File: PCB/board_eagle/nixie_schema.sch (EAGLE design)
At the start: 93 parts, among them Q1 BC856B, Q2 IRF740S, U2 MC7940N

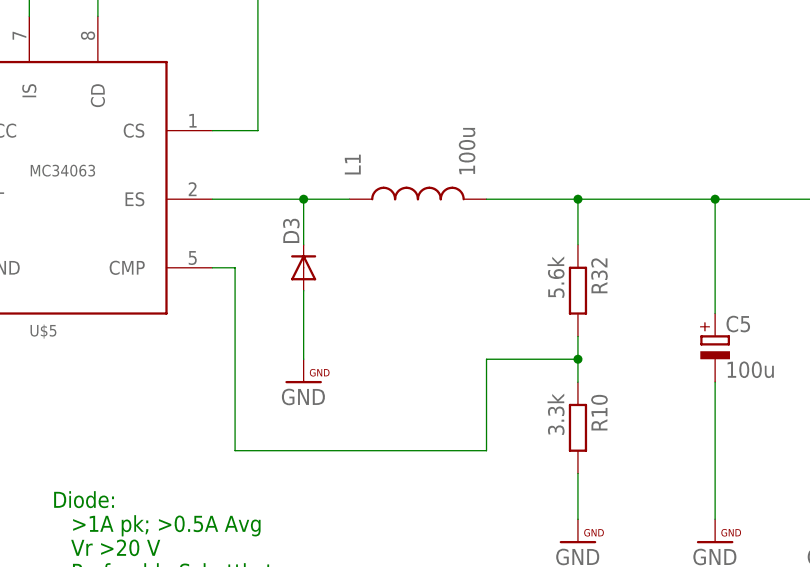
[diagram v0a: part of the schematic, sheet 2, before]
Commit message: Added some footprints
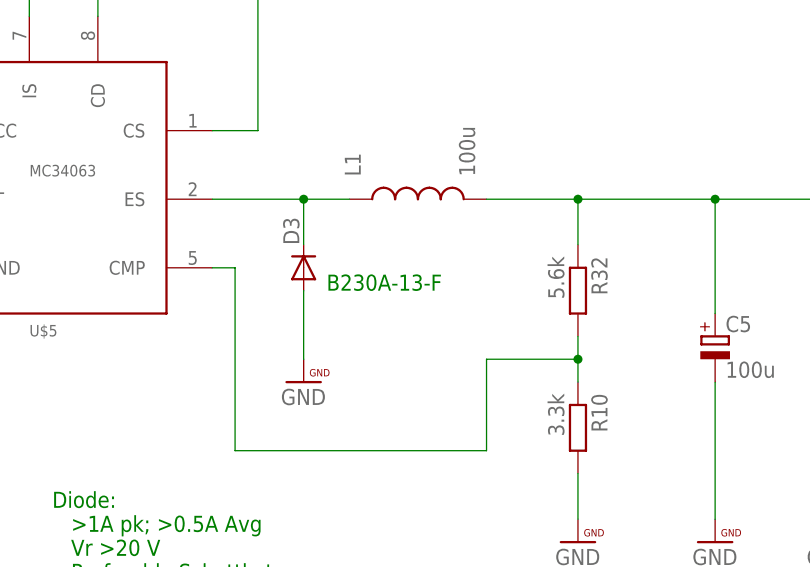
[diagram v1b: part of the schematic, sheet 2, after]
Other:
- note added: "B230A-13-F"
- note added: "ECS-.327-7-34B"
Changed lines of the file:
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@@
    &gt;0.5A cont, &gt;1A peak
    &gt;=100 uH</text>
+<text x="83.82" y="58.42" size="1.778" layer="91">
+B230A-13-F
+</text>
 </plain>
 <instances>
@@
 Note:
    Populate either R8 or R28, not both</text>
+<text x="266.7" y="0" size="1.778" layer="91">
+ECS-.327-7-34B
+</text>
 </plain>
 <instances>

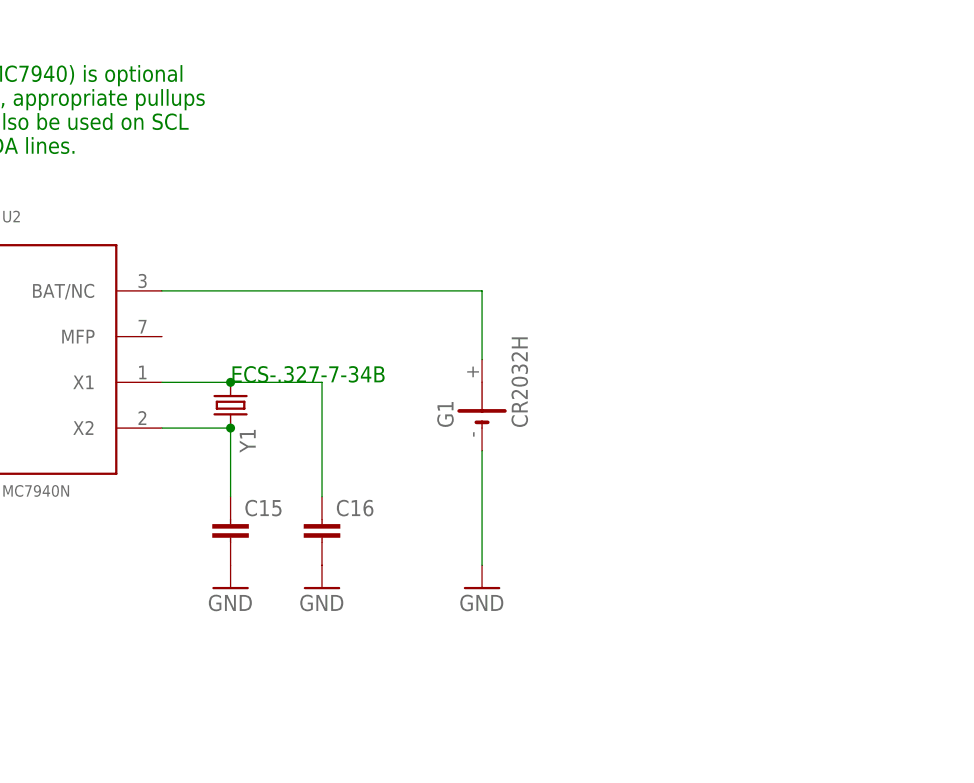
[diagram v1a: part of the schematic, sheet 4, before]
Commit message: Added some more component footprints
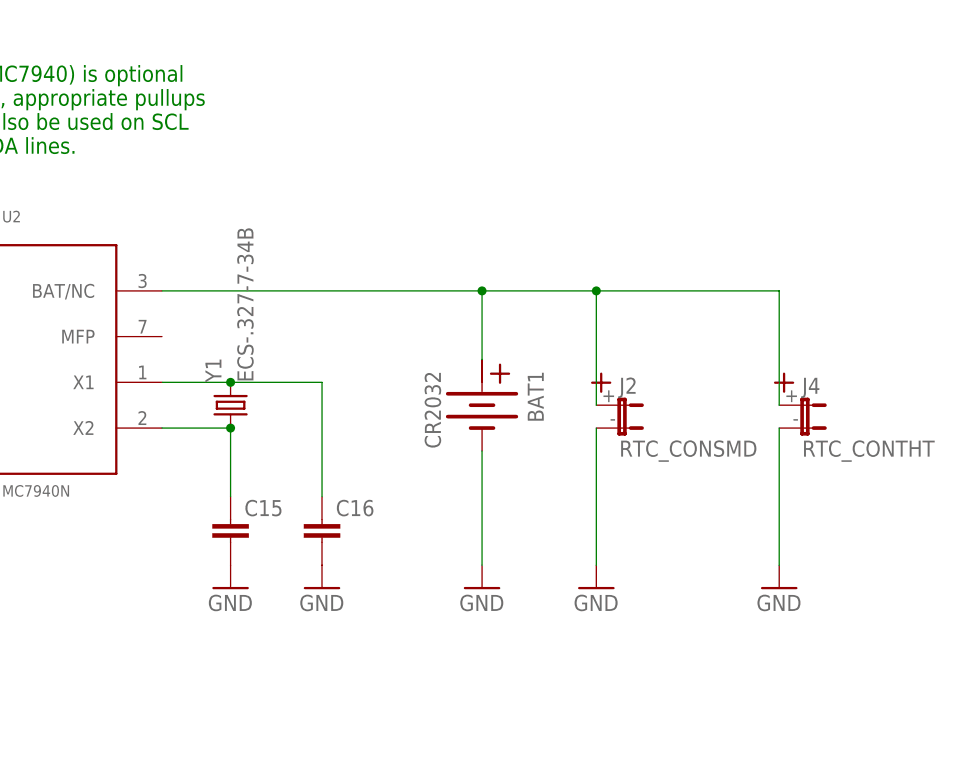
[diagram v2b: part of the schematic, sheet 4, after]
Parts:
- removed G1: CR2032H, battery:CR2032H
- added BAT1: CR2032, nixe_cmp:CR2032
- added D4: B230A-13-F, nixe_cmp:B230A-13-F
- added J2: RTC_CONSMD, nixe_cmp:RTC_CONSMD
- added J4: RTC_CONTHT, nixe_cmp:RTC_CONTHT
- added J5: (no value), con-jack:JACK-PLUG0
- D3: value (none) -> B230A-13-F; device diode:DIODE-SOD123 -> nixe_cmp:B230A-13-F
- Y1: value (none) -> ECS-.327-7-34B; device crystal:CRYSTALSM49 -> nixe_cmp:ECS-.327-7-34B
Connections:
- new net N$93: D4.A, J5.3
- net GND: now also BAT1.-, J2.-, J4.-, J5.1, J5.2; no longer G1.-
- net N$100: now also Y1.1; no longer Y1.2
- net N$22: now also BAT1.+, J2.+, J4.+; no longer G1.+
- net N$99: now also Y1.2; no longer Y1.1
- net VCC: now also D4.C
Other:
- note removed: "B230A-13-F"
- note removed: "ECS-.327-7-34B"
- moved on the sheet: Y1
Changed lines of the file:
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@@
 <part name="U$8" library="PatternAgents-Beautify" deviceset="GND" device=""/>
 <part name="U$9" library="PatternAgents-Beautify" deviceset="GND" device=""/>
-<part name="D3" library="diode" deviceset="DIODE-" device="SOD123"/>
 <part name="C6" library="rcl" deviceset="CPOL-EU" device="153CLV-1014" value="100u"/>
 <part name="U$10" library="PatternAgents-Beautify" deviceset="GND" device=""/>
@@
 <part name="U2" library="nixe_cmp" deviceset="MC7940" device="" technology="N"/>
 <part name="GND11" library="supply1" deviceset="GND" device=""/>
-<part name="G1" library="battery" deviceset="CR2032H" device=""/>
 <part name="GND12" library="supply1" deviceset="GND" device=""/>
 <part name="GND13" library="supply1" deviceset="GND" device=""/>
 <part name="U$11" library="PatternAgents-Beautify" deviceset="GND" device=""/>
 <part name="U$12" library="PatternAgents-Beautify" deviceset="GND" device=""/>
-<part name="Y1" library="crystal" deviceset="CRYSTAL" device="SM49"/>
 <part name="C15" library="rcl" deviceset="C-EU" device="C0805"/>
 <part name="C16" library="rcl" deviceset="C-EU" device="C0805"/>
@@
 <part name="U$31" library="PatternAgents-Beautify" deviceset="GND" device=""/>
 <part name="R8" library="resistor" deviceset="R-EU_" device="R0603"/>
+<part name="Y1" library="nixe_cmp" deviceset="ECS-.327-7-34B" device=""/>
+<part name="BAT1" library="nixe_cmp" deviceset="CR2032" device=""/>
+<part name="J2" library="nixe_cmp" deviceset="RTC_CON" device="SMD"/>
+<part name="J4" library="nixe_cmp" deviceset="RTC_CON" device="THT"/>
+<part name="GND16" library="supply1" deviceset="GND" device=""/>
+<part name="GND17" library="supply1" deviceset="GND" device=""/>
+<part name="SUPPLY6" library="SparkFun-PowerSymbols" deviceset="VCC" device=""/>
+<part name="D3" library="nixe_cmp" deviceset="B230A-13-F" device=""/>
+<part name="D4" library="nixe_cmp" deviceset="B230A-13-F" device=""/>
+<part name="J5" library="con-jack" deviceset="JACK-PLUG" device="0"/>
+<part name="U$32" library="PatternAgents-Beautify" deviceset="GND" device=""/>
 </parts>
 <sheets>
@@
    &gt;0.5A cont, &gt;1A peak
    &gt;=100 uH</text>
-<text x="83.82" y="58.42" size="1.778" layer="91">
-B230A-13-F
-</text>
 </plain>
 <instances>
@@
 <instance part="U$8" gate="G$1" x="111.76" y="33.02"/>
 <instance part="U$9" gate="G$1" x="81.28" y="50.8"/>
-<instance part="D3" gate="G$1" x="81.28" y="60.96" rot="R90"/>
 <instance part="C6" gate="G$1" x="139.7" y="53.34"/>
 <instance part="U$10" gate="G$1" x="139.7" y="33.02"/>
@@
 <instance part="C8" gate="G$1" x="0" y="53.34"/>
 <instance part="C4" gate="G$1" x="12.7" y="53.34"/>
+<instance part="SUPPLY6" gate="G$1" x="-10.16" y="111.76"/>
+<instance part="D3" gate="G$1" x="81.28" y="60.96" rot="R90"/>
+<instance part="D4" gate="G$1" x="-25.4" y="83.82"/>
+<instance part="J5" gate="G$1" x="-45.72" y="81.28"/>
+<instance part="U$32" gate="G$1" x="-35.56" y="33.02"/>
 </instances>
 <busses>
@@
 <segment>
 <pinref part="U$9" gate="G$1" pin="GND"/>
+<wire x1="81.28" y1="50.8" x2="81.28" y2="58.42" width="0.1524" layer="91"/>
 <pinref part="D3" gate="G$1" pin="A"/>
-<wire x1="81.28" y1="50.8" x2="81.28" y2="58.42" width="0.1524" layer="91"/>
 </segment>
 <segment>
@@
 <wire x1="0" y1="33.02" x2="0" y2="48.26" width="0.1524" layer="91"/>
 </segment>
+<segment>
+<pinref part="U$32" gate="G$1" pin="GND"/>
+<wire x1="-35.56" y1="33.02" x2="-35.56" y2="78.74" width="0.1524" layer="91"/>
+<pinref part="J5" gate="G$1" pin="2"/>
+<wire x1="-35.56" y1="78.74" x2="-35.56" y2="81.28" width="0.1524" layer="91"/>
+<wire x1="-35.56" y1="81.28" x2="-40.64" y2="81.28" width="0.1524" layer="91"/>
+<pinref part="J5" gate="G$1" pin="1"/>
+<wire x1="-40.64" y1="78.74" x2="-35.56" y2="78.74" width="0.1524" layer="91"/>
+<junction x="-35.56" y="78.74"/>
+</segment>
 </net>
 <net name="N$12" class="0">
@@
 <pinref part="L1" gate="G$1" pin="1"/>
 <wire x1="71.12" y1="68.58" x2="81.28" y2="68.58" width="0.1524" layer="91"/>
-<pinref part="D3" gate="G$1" pin="C"/>
 <wire x1="81.28" y1="68.58" x2="86.36" y2="68.58" width="0.1524" layer="91"/>
 <wire x1="81.28" y1="63.5" x2="81.28" y2="68.58" width="0.1524" layer="91"/>
 <junction x="81.28" y="68.58"/>
+<pinref part="D3" gate="G$1" pin="C"/>
 </segment>
 </net>
@@
 <wire x1="0" y1="76.2" x2="12.7" y2="76.2" width="0.1524" layer="91"/>
 <junction x="12.7" y="76.2"/>
+</segment>
+<segment>
+<pinref part="SUPPLY6" gate="G$1" pin="VCC"/>
+<wire x1="-22.86" y1="83.82" x2="-10.16" y2="83.82" width="0.1524" layer="91"/>
+<wire x1="-10.16" y1="83.82" x2="-10.16" y2="111.76" width="0.1524" layer="91"/>
+<pinref part="D4" gate="G$1" pin="C"/>
+</segment>
+</net>
+<net name="N$93" class="0">
+<segment>
+<pinref part="J5" gate="G$1" pin="3"/>
+<pinref part="D4" gate="G$1" pin="A"/>
+<wire x1="-40.64" y1="83.82" x2="-27.94" y2="83.82" width="0.1524" layer="91"/>
 </segment>
 </net>
@@
 Note:
    Populate either R8 or R28, not both</text>
-<text x="266.7" y="0" size="1.778" layer="91">
-ECS-.327-7-34B
-</text>
 </plain>
 <instances>
@@
 <instance part="U2" gate="G$1" x="243.84" y="2.54"/>
 <instance part="GND11" gate="1" x="226.06" y="-22.86"/>
-<instance part="G1" gate="1" x="294.64" y="-2.54" rot="R90"/>
 <instance part="GND12" gate="1" x="294.64" y="-22.86"/>
 <instance part="GND13" gate="1" x="215.9" y="7.62"/>
-<instance part="Y1" gate="G$1" x="266.7" y="-2.54" rot="R270"/>
 <instance part="C15" gate="G$1" x="266.7" y="-15.24"/>
 <instance part="C16" gate="G$1" x="276.86" y="-15.24"/>
@@
 <instance part="U$31" gate="G$1" x="-15.24" y="35.56"/>
 <instance part="R8" gate="G$1" x="73.66" y="76.2" rot="R270"/>
+<instance part="Y1" gate="G$1" x="266.7" y="-2.54" rot="R90"/>
+<instance part="BAT1" gate="G$1" x="294.64" y="-2.54" rot="R270"/>
+<instance part="J2" gate="G$1" x="309.88" y="-2.54" rot="R270"/>
+<instance part="J4" gate="G$1" x="330.2" y="-2.54" rot="R270"/>
+<instance part="GND16" gate="1" x="307.34" y="-22.86"/>
+<instance part="GND17" gate="1" x="327.66" y="-22.86"/>
 </instances>
 <busses>
@@
 <segment>
 <pinref part="GND12" gate="1" pin="GND"/>
-<pinref part="G1" gate="1" pin="-"/>
 <wire x1="294.64" y1="-20.32" x2="294.64" y2="-7.62" width="0.1524" layer="91"/>
+<pinref part="BAT1" gate="G$1" pin="-"/>
 </segment>
 <segment>
@@
 <pinref part="C18" gate="G$1" pin="2"/>
 <wire x1="-15.24" y1="35.56" x2="-15.24" y2="40.64" width="0.1524" layer="91"/>
+</segment>
+<segment>
+<pinref part="GND16" gate="1" pin="GND"/>
+<pinref part="J2" gate="G$1" pin="-"/>
+<wire x1="307.34" y1="-20.32" x2="307.34" y2="-5.08" width="0.1524" layer="91"/>
+</segment>
+<segment>
+<pinref part="J4" gate="G$1" pin="-"/>
+<pinref part="GND17" gate="1" pin="GND"/>
+<wire x1="327.66" y1="-5.08" x2="327.66" y2="-20.32" width="0.1524" layer="91"/>
 </segment>
 </net>
@@
 <net name="N$22" class="0">
 <segment>
-<pinref part="G1" gate="1" pin="+"/>
 <wire x1="294.64" y1="2.54" x2="294.64" y2="10.16" width="0.1524" layer="91"/>
 <pinref part="U2" gate="G$1" pin="BAT/NC"/>
 <wire x1="294.64" y1="10.16" x2="259.08" y2="10.16" width="0.1524" layer="91"/>
+<pinref part="BAT1" gate="G$1" pin="+"/>
+<pinref part="J2" gate="G$1" pin="+"/>
+<wire x1="307.34" y1="-2.54" x2="307.34" y2="10.16" width="0.1524" layer="91"/>
+<wire x1="307.34" y1="10.16" x2="294.64" y2="10.16" width="0.1524" layer="91"/>
+<junction x="294.64" y="10.16"/>
+<pinref part="J4" gate="G$1" pin="+"/>
+<wire x1="307.34" y1="10.16" x2="327.66" y2="10.16" width="0.1524" layer="91"/>
+<wire x1="327.66" y1="10.16" x2="327.66" y2="-2.54" width="0.1524" layer="91"/>
+<junction x="307.34" y="10.16"/>
 </segment>
 </net>
@@
 <segment>
 <pinref part="U2" gate="G$1" pin="X1"/>
-<pinref part="Y1" gate="G$1" pin="1"/>
-<wire x1="259.08" y1="0" x2="266.7" y2="0" width="0.1524" layer="91"/>
 <pinref part="C16" gate="G$1" pin="1"/>
 <wire x1="276.86" y1="-12.7" x2="276.86" y2="0" width="0.1524" layer="91"/>
 <wire x1="276.86" y1="0" x2="266.7" y2="0" width="0.1524" layer="91"/>
+<pinref part="Y1" gate="G$1" pin="2"/>
+<wire x1="266.7" y1="0" x2="259.08" y2="0" width="0.1524" layer="91"/>
 <junction x="266.7" y="0"/>
 </segment>
@@
 <segment>
 <pinref part="U2" gate="G$1" pin="X2"/>
-<pinref part="Y1" gate="G$1" pin="2"/>
 <wire x1="259.08" y1="-5.08" x2="266.7" y2="-5.08" width="0.1524" layer="91"/>
 <pinref part="C15" gate="G$1" pin="1"/>
 <wire x1="266.7" y1="-12.7" x2="266.7" y2="-5.08" width="0.1524" layer="91"/>
+<pinref part="Y1" gate="G$1" pin="1"/>
 <junction x="266.7" y="-5.08"/>
 </segment>

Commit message: Starting to do layout
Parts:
- C2: device rcl:CPOL-EU140CLH-0810 -> rcl:C-EUC0805
- S1, S2, S3, S4, S5, S6: value TAC_SWITCHSMD -> (none); device SparkFun-Retired:TAC_SWITCHSMD -> switch-omron:31-XX
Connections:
- net N$86 renamed V_PULSE
- new net N$94: SV7.11
- net +3V3: now also C7.1
- net BUTTON1: now also S3.S; no longer S2.3, S2.4
- net BUTTON2: now also S4.S; no longer S3.3, S3.4
- net BUTTON3: now also S5.S; no longer S4.3, S4.4
- net BUTTON4: now also S6.S; no longer S5.3, S5.4
- net GND: now also C1.2, C10.2, C11.2, C14.2, C2.2, C3.2, C4.2, C8.2, S1.P, S2.P, S3.P, S4.P, S5.P, S6.P; no longer C2.-, S1.1, S1.2, S2.1, S2.2, S3.1, S3.2, S4.1, S4.2, S5.1, S5.2, S6.3, S6.4
- net N$10: no longer SV7.11
- net N$12: now also C4.1
- net N$14: now also S1.S; no longer S1.3, S1.4
- net N$15: now also S2.S; no longer S6.1, S6.2
- net N$74: now also C10.1
- net N$96: now also C11.1
- net VCC: now also C1.1, C14.1, C2.1, C3.1, C8.1; no longer C2.+

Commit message: Some more routing
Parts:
- C12: device rcl:CPOL-EU153CLV-0810 -> rcl:CPOL-EU153CLV-1014
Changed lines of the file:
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@@
 </variantdefs>
 <classes>
-<class number="0" name="default" width="0.1524" drill="0.4064">
-<clearance class="0" value="0.1524"/>
+<class number="0" name="default" width="0.254" drill="0.4">
+<clearance class="0" value="0.2032"/>
 </class>
-<class number="1" name="Power" width="1.016" drill="0.4064">
+<class number="1" name="Power" width="1.016" drill="0.5">
 </class>
-<class number="2" name="HV" width="0.1524" drill="0.4064">
-<clearance class="2" value="0.508"/>
+<class number="2" name="HV" width="0.254" drill="0.5">
+<clearance class="2" value="1"/>
 </class>
 </classes>
@@
 <part name="Q1" library="nixe_cmp" deviceset="BC856B" device=""/>
 <part name="L3" library="nixe_cmp" deviceset="HM78D-128151KLFTR" device="" value="150u"/>
-<part name="C12" library="rcl" deviceset="CPOL-EU" device="153CLV-0810" value="220u"/>
 <part name="C13" library="rcl" deviceset="CPOL-EU" device="153CLV-1014" value="2.2u"/>
 <part name="R27" library="pot" deviceset="TRIM_EU-" device="SM-42/43X" value="100k"/>
@@
 <part name="S1" library="switch-omron" deviceset="31-XX" device=""/>
 <part name="C2" library="rcl" deviceset="C-EU" device="C0805" value="100n"/>
+<part name="C12" library="rcl" deviceset="CPOL-EU" device="153CLV-1014" value="220u"/>
 </parts>
 <sheets>
@@
 <instance part="Q1" gate="Q$1" x="96.52" y="25.4"/>
 <instance part="L3" gate="G$1" x="119.38" y="66.04"/>
-<instance part="C12" gate="G$1" x="88.9" y="66.04"/>
 <instance part="C13" gate="G$1" x="218.44" y="17.78"/>
 <instance part="R27" gate="1" x="200.66" y="17.78"/>
@@
 <instance part="C10" gate="G$1" x="10.16" y="22.86"/>
 <instance part="C11" gate="G$1" x="160.02" y="20.32"/>
+<instance part="C12" gate="G$1" x="88.9" y="66.04"/>
 </instances>
 <busses>

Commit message: Routing the PCB
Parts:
- removed C2: 100n, rcl:C-EUC0805
- removed C9: 10u, rcl:CPOL-EU140CLH-0810
- added P1: 100k, nixe_cmp:UNIVERSAL-POTENTIOMETER_SMD
- added R31, R33, R34, R35: 68k, rcl:R-EU_R0603
- added R36: (no value), resistor:R-EU_R0603
- added T1: PHOTO_TRANS, nixe_cmp:PHOTO_TRANS
- R27: value 100k -> (none); device pot:TRIM_EU-SM-42/43X -> resistor:R-EU_R0603
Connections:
- net N$1 renamed HV_DATA_IN
- net N$2 renamed HV_LE
- net N$6 renamed HV_DATA_CLK
- net N$7 renamed HV_DATA_OUT
- new net HV_HA_DP: R31.2, U$1.HV31
- new net HV_HB_DP: R33.2, U$1.HV32
- new net HV_MA_DP: R34.2, U$2.HV31
- new net HV_MB_DP: R35.2, U$2.HV32
- new net N$101: N3.LHDP, SV9.11
- new net N$102: N4.LHDP, SV10.11
- new net N$104: N6.LHDP, SV12.11
- new net N$105: N5.LHDP, SV11.11
- new net N$106: R31.1, SV1.11
- new net N$108: R33.1, SV2.11
- new net N$110: R34.1, SV3.11
- new net N$112: R35.1, SV4.11
- new net N$86: N2.LHDP, SV8.11
- new net PHOTO: R27.2, T1.C, U1.ADC
- net +3V3: now also R27.1; no longer C9.+
- net GND: now also P1.WIPER, R36.2; no longer C2.2, C9.-, R27.S
- net HV_MA_8: now also U$1.HV29
- net HV_MA_9: now also U$1.HV30; no longer U$1.HV29
- net N$109: now also R36.1, T1.E; no longer U$1.HV30
- net N$11: no longer SV3.11
- net N$19: no longer SV8.11
- net N$21: no longer SV9.11
- net N$45: no longer SV12.11
- net N$8: no longer SV4.11
- net N$88: no longer SV10.11
- net N$89: no longer SV1.11
- net N$90: no longer SV2.11
- net N$91: no longer SV6.11
- net N$92: no longer SV5.11
- net N$94: now also N1.LHDP
- net N$97: now also P1.E; no longer R27.E
- net N$98: no longer SV11.11
- net VCC: no longer C2.1
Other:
- moved on the sheet: N2, N3, N4, N5, N6, SV10, SV11, SV12, SV8, SV9

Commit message: Gottom board routing mostly done
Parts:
- added C2: 100n, rcl:C-EUC0805
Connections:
- net GND: now also C2.2
- net HV_HA_DP: now also U$1.HV11; no longer U$1.HV31
- net HV_HB_0: now also U$1.HV18; no longer U$1.HV11
- net HV_HB_1: now also U$1.HV19; no longer U$1.HV12
- net HV_HB_2: now also U$1.HV20; no longer U$1.HV13
- net HV_HB_3: now also U$1.HV21; no longer U$1.HV15
- net HV_HB_4: now also U$1.HV22; no longer U$1.HV14
- net HV_HB_6: now also U$1.HV15; no longer U$1.HV17
- net HV_HB_7: now also U$1.HV14; no longer U$1.HV18
- net HV_HB_8: now also U$1.HV13; no longer U$1.HV19
- net HV_HB_9: now also U$1.HV12; no longer U$1.HV20
- net HV_HB_DP: now also U$1.HV17; no longer U$1.HV32
- net HV_MA_0: now also U$1.HV27; no longer U$1.HV21
- net HV_MA_1: now also U$1.HV26; no longer U$1.HV22
- net HV_MA_2: now also U$1.HV25; no longer U$1.HV23
- net HV_MA_4: now also U$1.HV23; no longer U$1.HV25
- net HV_MA_5: now also U$1.HV28; no longer U$1.HV26
- net HV_MA_6: now also U$1.HV29; no longer U$1.HV27
- net HV_MA_7: now also U$1.HV30; no longer U$1.HV28
- net HV_MA_8: now also U$1.HV31; no longer U$1.HV29
- net HV_MA_9: now also U$1.HV32; no longer U$1.HV30
- net HV_MA_DP: now also U$2.HV12; no longer U$2.HV31
- net HV_MB_0: now also U$2.HV5; no longer U$2.HV1
- net HV_MB_1: now also U$2.HV4; no longer U$2.HV2
- net HV_MB_3: now also U$2.HV2; no longer U$2.HV4
- net HV_MB_4: now also U$2.HV1; no longer U$2.HV5
- net HV_MB_5: now also U$2.HV7; no longer U$2.HV6
- net HV_MB_6: now also U$2.HV8; no longer U$2.HV7
- net HV_MB_7: now also U$2.HV9; no longer U$2.HV8
- net HV_MB_8: now also U$2.HV10; no longer U$2.HV9
- net HV_MB_9: now also U$2.HV11; no longer U$2.HV10
- net HV_MB_DP: now also U$2.HV6; no longer U$2.HV32
- net HV_SA_0: now also U$2.HV18; no longer U$2.HV11
- net HV_SA_1: now also U$2.HV19; no longer U$2.HV12
- net HV_SA_2: now also U$2.HV20; no longer U$2.HV13
- net HV_SA_3: now also U$2.HV21; no longer U$2.HV15
- net HV_SA_4: now also U$2.HV22; no longer U$2.HV14
- net HV_SA_5: now also U$2.HV17; no longer U$2.HV16
- net HV_SA_6: now also U$2.HV16; no longer U$2.HV17
- net HV_SA_7: now also U$2.HV15; no longer U$2.HV18
- net HV_SA_8: now also U$2.HV14; no longer U$2.HV19
- net HV_SA_9: now also U$2.HV13; no longer U$2.HV20
- net HV_SB_0: now also U$2.HV27; no longer U$2.HV21
- net HV_SB_1: now also U$2.HV26; no longer U$2.HV22
- net HV_SB_2: now also U$2.HV25; no longer U$2.HV23
- net HV_SB_4: now also U$2.HV23; no longer U$2.HV25
- net HV_SB_5: now also U$2.HV32; no longer U$2.HV26
- net HV_SB_6: now also U$2.HV31; no longer U$2.HV27
- net HV_SB_7: now also U$2.HV30; no longer U$2.HV28
- net HV_SB_9: now also U$2.HV28; no longer U$2.HV30
- net VCC: now also C2.1
